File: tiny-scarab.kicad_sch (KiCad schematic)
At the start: 28 parts, among them J3 Conn_02x07_Odd_Even, J4 Conn_02x07_Odd_Even, J5 Screw_Hole, J6 Screw_Hole, J7 Screw_Hole, J8 Screw_Hole

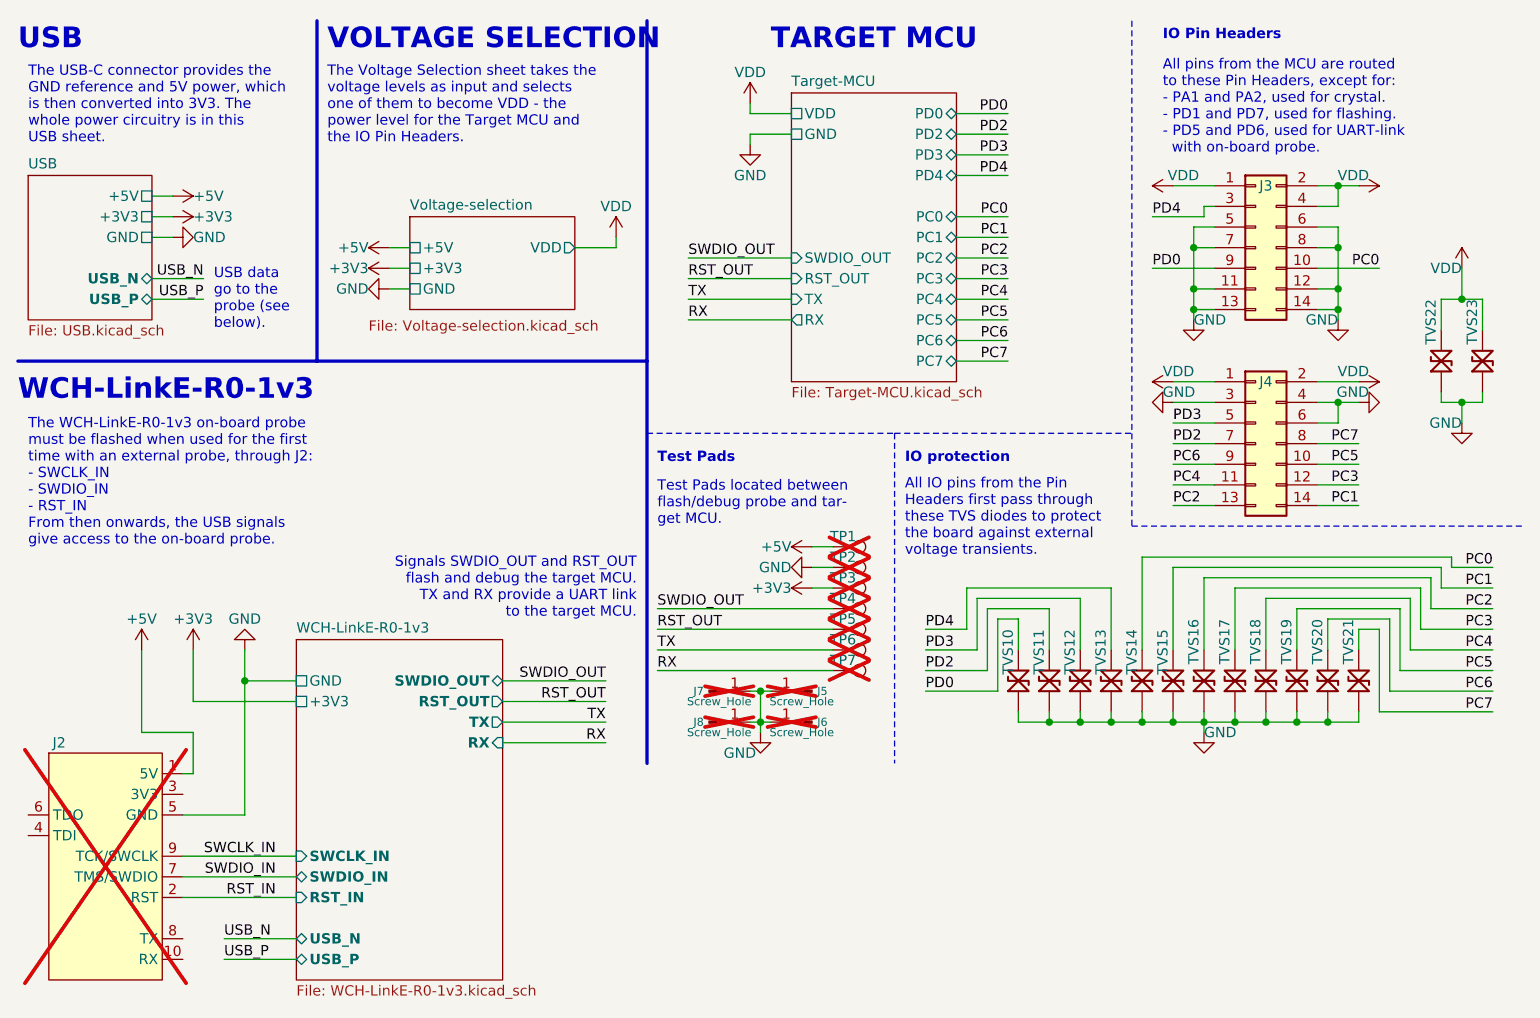
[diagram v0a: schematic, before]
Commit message: Replace TVS diodes with cheaper alternative
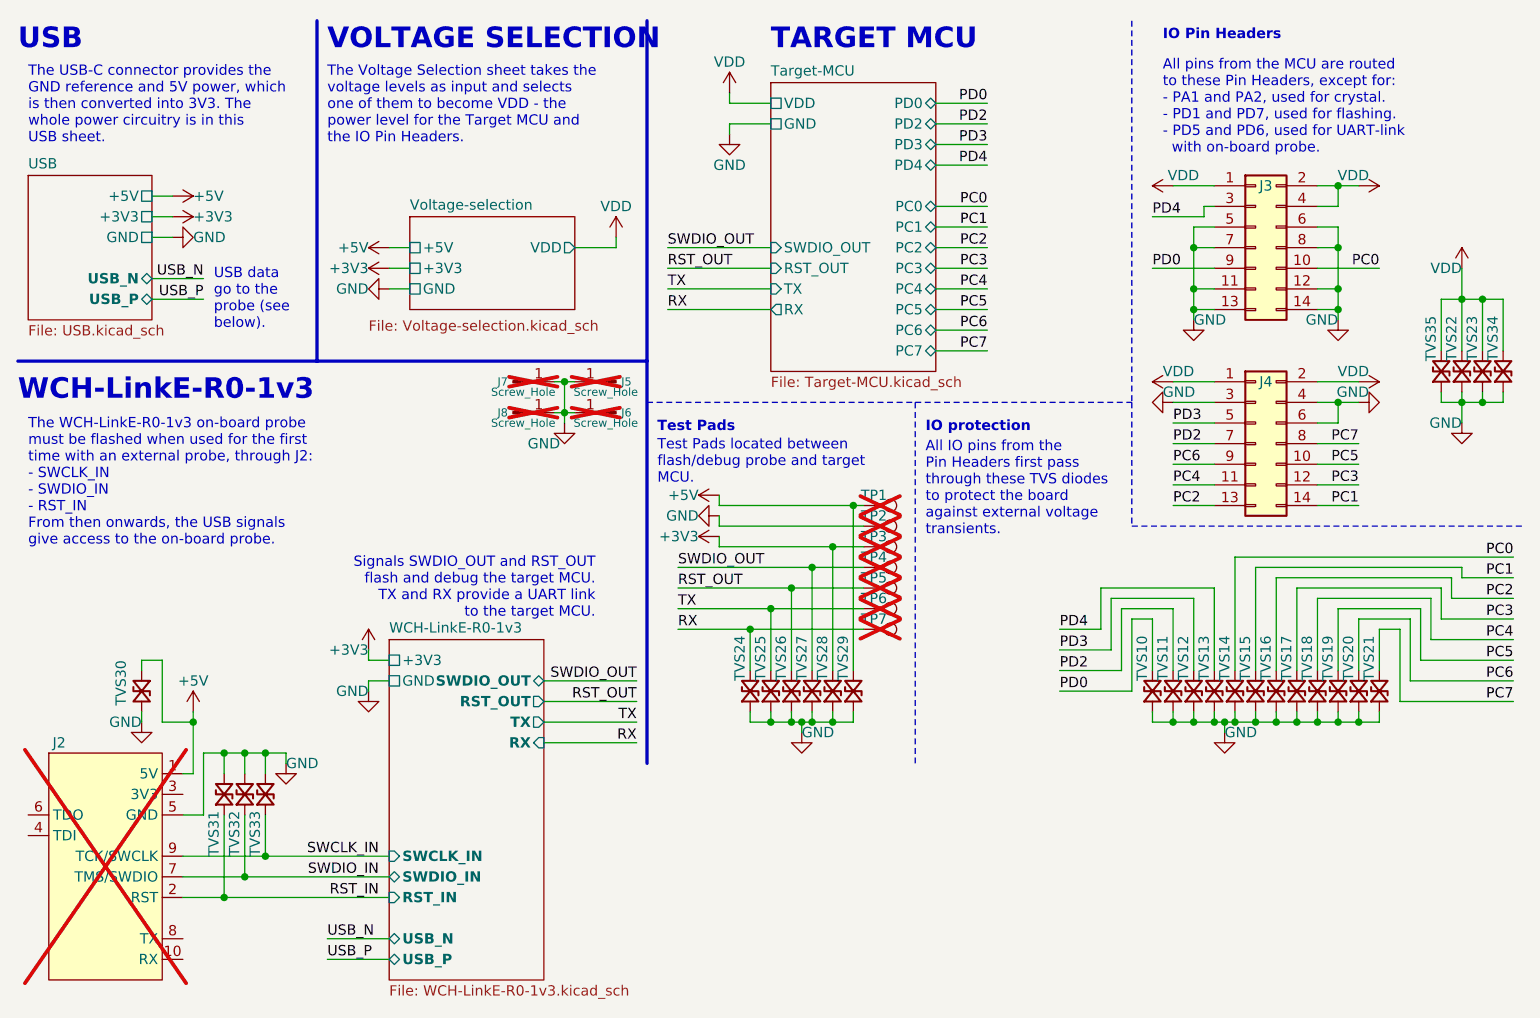
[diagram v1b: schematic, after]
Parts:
- removed TVS10, TVS11, TVS12, TVS13, TVS14, TVS15, TVS16, TVS17, TVS18, TVS19, TVS20, TVS21, TVS22, TVS23: 5V, Tiny_Scarab:D_SOD-323_CDSOD323-T05LC, symbol Tiny_Scarab:CDSOD323-T05LC
- added TVS10, TVS11, TVS12, TVS13, TVS14, TVS15, TVS16, TVS17, TVS18, TVS19, TVS20, TVS21, TVS22, TVS23, TVS24, TVS25, TVS26, TVS27, TVS28, TVS29, TVS30, TVS31, TVS32, TVS33, TVS34, TVS35: 5V, Tiny_Scarab:D_SOD-882_SP1007-01ETG, symbol Tiny_Scarab:TVS_SP1007-01ETG
- J3: MPN 10129383-914001ALF -> C84004; Manufacturer Amphenol ICC (FCI) -> BOOMELE(Boom Precision Elec); SPN 10129383-914001ALF-ND -> (none); Supplier DigiKey -> (none)
- J4: MPN 10129383-914001ALF -> C84004; Manufacturer Amphenol ICC (FCI) -> BOOMELE(Boom Precision elec); SPN 10129383-914001ALF-ND -> (none); Supplier DigiKey -> (none)
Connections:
- net +3V3: now also TVS28.1
- net +5V: now also TVS29.1, TVS30.2
- net GND: now also TVS10.2, TVS11.2, TVS12.2, TVS13.2, TVS14.2, TVS15.2, TVS16.2, TVS17.2, TVS18.2, TVS19.2, TVS20.2, TVS21.2, TVS22.2, TVS23.2, TVS24.2, TVS25.2, TVS26.2, TVS27.2, TVS28.2, TVS29.2, TVS30.1, TVS31.1, TVS32.1, TVS33.1, TVS34.2, TVS35.2
- net PC0: now also TVS14.1
- net PC1: now also TVS15.1
- net PC2: now also TVS16.1
- net PC3: now also TVS17.1
- net PC4: now also TVS18.1
- net PC5: now also TVS19.1
- net PC6: now also TVS20.1
- net PC7: now also TVS21.1
- net PD0: now also TVS10.1
- net PD2: now also TVS11.1
- net PD3: now also TVS12.1
- net PD4: now also TVS13.1
- net RST_IN: now also TVS31.2
- net RST_OUT: now also TVS26.1
- net RX: now also TVS24.1
- net SWCLK_IN: now also TVS33.2
- net SWDIO_IN: now also TVS32.2
- net SWDIO_OUT: now also TVS27.1
- net TX: now also TVS25.1
- net VDD: now also TVS22.1, TVS23.1, TVS34.1, TVS35.1
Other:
- note added: "Test Pads located between flash/debug probe and target MCU."
- note removed: "Test Pads located between flash/debug probe and tar- get MCU."
- moved on the sheet: J5, J6, J7, J8, TP1, TP2, TP3, TP4, TP5, TP6, TP7

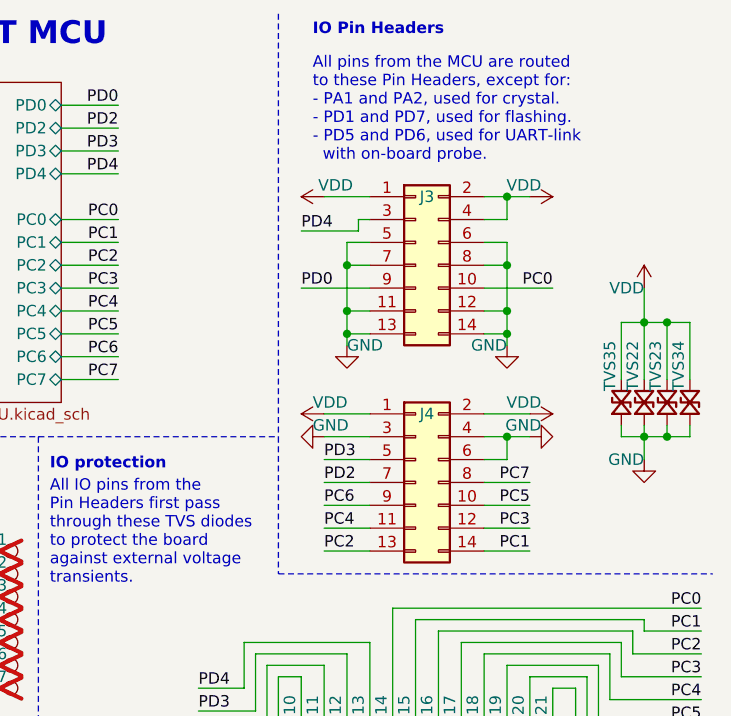
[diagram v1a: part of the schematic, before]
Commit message: Clean up symbols library
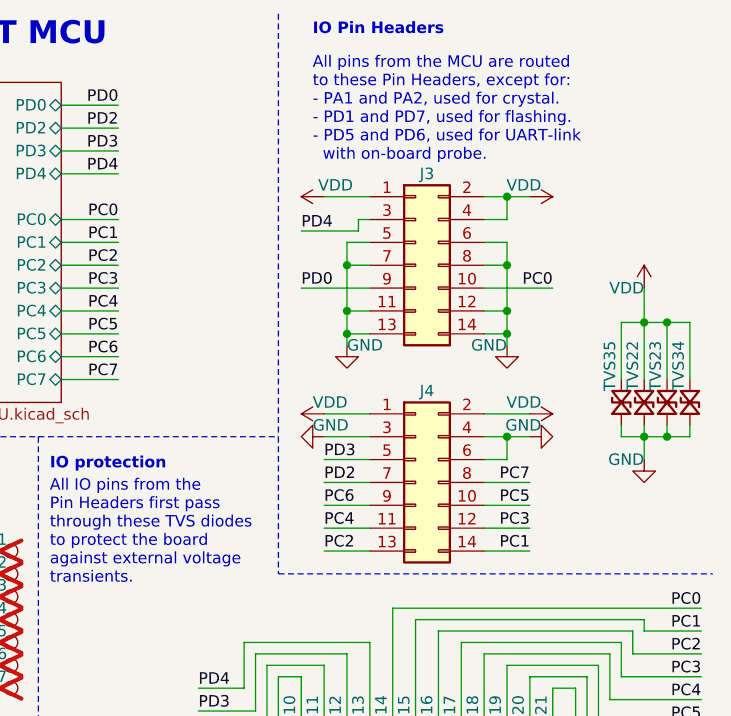
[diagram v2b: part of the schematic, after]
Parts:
- J2: DigiKey (none) -> TC2050-IDC-NL-ND
- J3: SPN (none) -> 10129383-914001ALF-ND; Supplier (none) -> DigiKey
- J4: Manufacturer BOOMELE(Boom Precision elec) -> BOOMELE(Boom Precision Elec); SPN (none) -> 10129383-914001ALF-ND; Supplier (none) -> DigiKey
- TVS10, TVS11, TVS12, TVS13, TVS14, TVS15, TVS16, TVS17, TVS18, TVS19, TVS20, TVS21, TVS22, TVS23, TVS24, TVS25, TVS26, TVS27, TVS28, TVS29, TVS30, TVS31, TVS32, TVS33, TVS34, TVS35: Farnell (none) -> 2777317; Mouser (none) -> 576-SP1007-01ETG
